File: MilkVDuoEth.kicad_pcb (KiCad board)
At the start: 2 copper layers, 18.8 x 26.8 mm, 6 parts, among them J1 Conn_01x05_Female, J2 RJ45-TRANSFORMER_LED_HANRUN

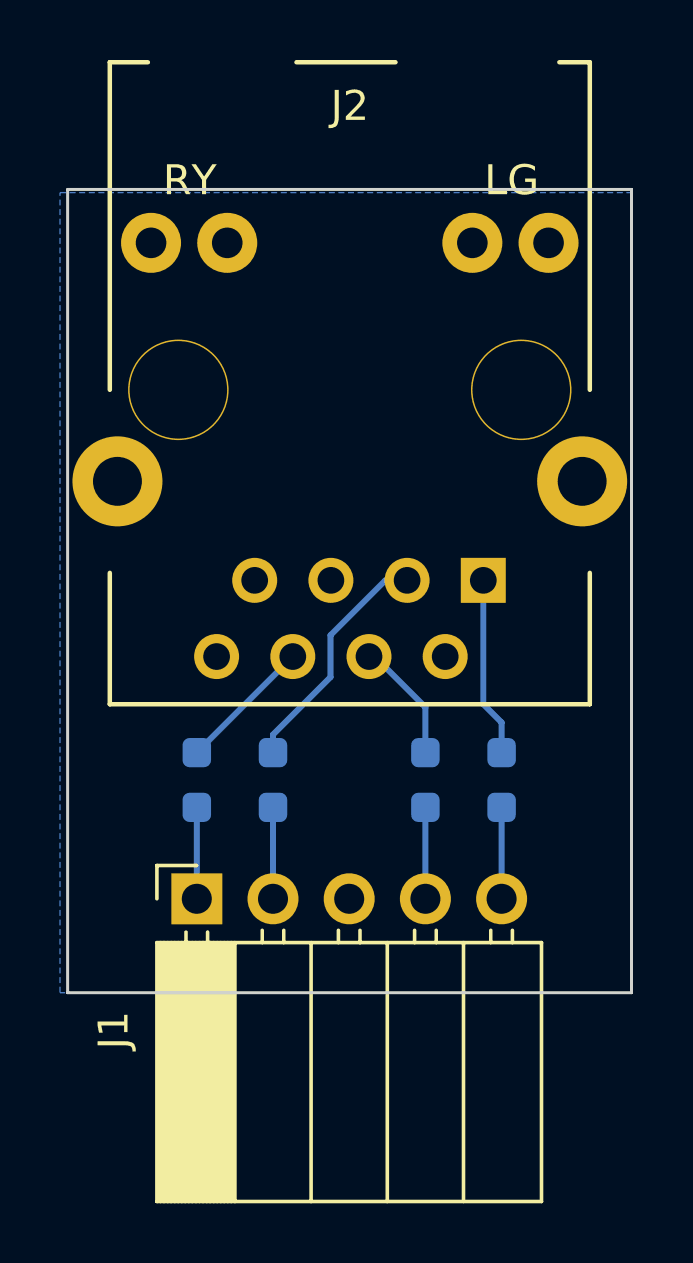
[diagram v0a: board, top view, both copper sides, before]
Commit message: Remove all SMT components from PCB.
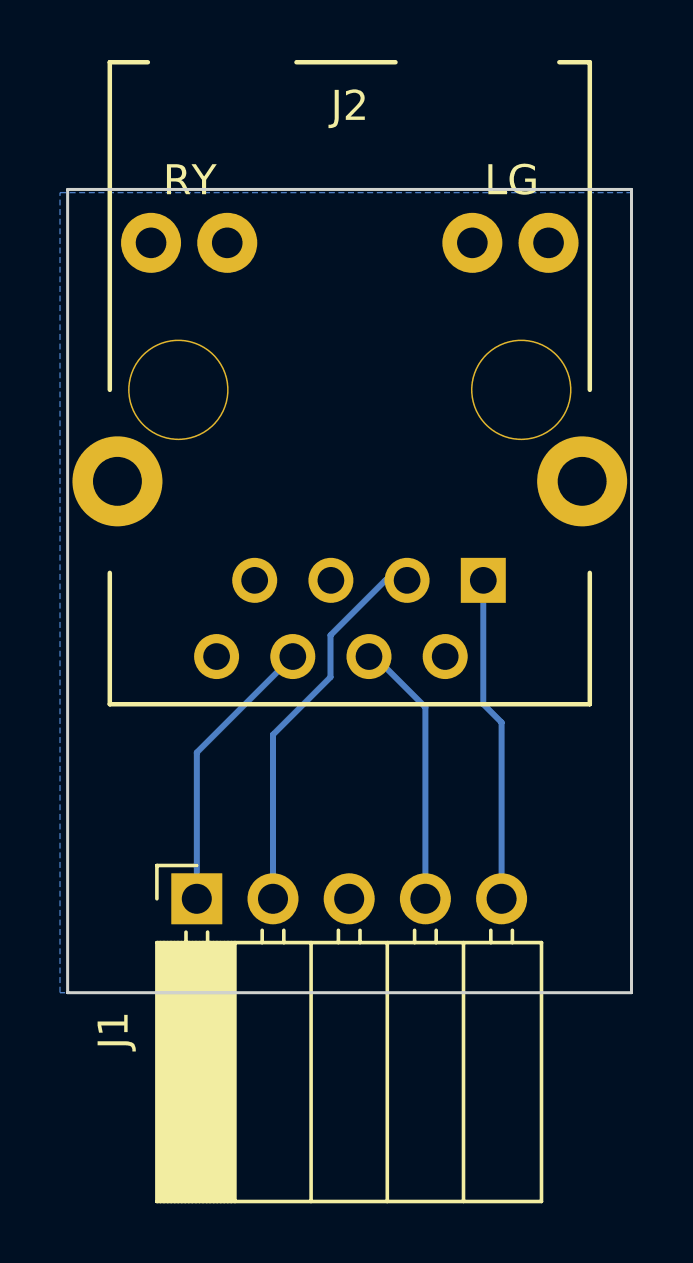
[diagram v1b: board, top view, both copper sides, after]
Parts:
- removed R1, R2, R3, R4: 5R1, Resistor_SMD:R_0603_1608Metric_Pad0.98x0.95mm_HandSolder
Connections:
- J1 pad 1: /MRD- -> /RD-
- J1 pad 2: /MRD+ -> /RD+
- J1 pad 4: /MTD- -> /TD-
- J1 pad 5: /MTD+ -> /TD+
- J2 pad 1: /ETD+ -> /TD+
- J2 pad 3: /ERD+ -> /RD+
- J2 pad 4: /ETD- -> /TD-
- J2 pad 6: /ERD- -> /RD-
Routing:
- net /RD+: track 0.00 -> 12.9 mm
- net /TD+: track 0.00 -> 10.9 mm
- net /RD-: track 0.00 -> 9.40 mm
- net /TD-: track 0.00 -> 8.97 mm
- net /ERD+: track 8.02 -> 0.00 mm
- net /ETD+: track 6.00 -> 0.00 mm
- net /ERD-: track 4.53 -> 0.00 mm
- net /ETD-: track 4.09 -> 0.00 mm
- net /MTD-: track 3.05 -> 0.00 mm
- net /MTD+: track 3.05 -> 0.00 mm
- net /MRD-: track 3.05 -> 0.00 mm
- net /MRD+: track 3.05 -> 0.00 mm
